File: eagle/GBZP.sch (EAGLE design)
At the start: 30 parts, among them CN1 Battery Connection, J1 AUDIO_JACK_3.5MM_SMD

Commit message: New Silk and New Case files
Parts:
- added C15, C18, C6, C7: 10u, rcl:C-EUC0805
- added C17: 100n, rcl:C-EUC0805
- added C5: 220n, rcl:C-EUC0805
- added C8: 330n, rcl:C-EUC0805
- added C9: 100uF, rcl:CPOL-EU153CLV-0405
- added R7: 27k, GBA:VOLUME
- added R8: 270R, rcl:R-EU_R0805
- added R9: 100k, rcl:R-EU_R0805
- added SP2: SPEAKER, GBA:SPEAKER
- added U4: LM4875, texas:LM4875
- added X2: HEADPHONE, GBA:HEADPHONE
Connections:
- removed net PWM_RIGHT: PI1.GPIO18, R3.1
- new net 5V: C15.1, C17.1, C18.1, C7.2, R7.E, R9.2, U4.VDD
- new net N$11: C6.1, U4.BYP
- new net N$13: C9.-, X2.LEFT, X2.RIGHT
- new net N$14: C9.+, SP2.+, U4.VOUT1
- new net N$15: SP2.-, U4.VOUT2
- new net N$16: R9.1, U4.HPHONE, X2.2
- new net N$5: C5.1, C8.1, R8.2
- new net N$8: R7.S, U4.DC_VOL
- new net N$9: C5.2, U4.VIN
- new net PWM: PI1.GPIO18, R3.1, R8.1
- net GND: now also C15.2, C17.2, C18.2, C6.2, C7.1, C8.2, R7.A, U4.GND, X2.1, X2.GND

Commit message: updates
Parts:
- removed C1: 10uF, adafruit:C-USC0805
- removed C15, C18, C6, C7: 10u, rcl:C-EUC0805
- removed C17: 100n, rcl:C-EUC0805
- removed C5: 220n, rcl:C-EUC0805
- removed C8: 330n, rcl:C-EUC0805
- removed C9: 100uF, rcl:CPOL-EU153CLV-0405
- removed R4: 270Ohm, adafruit:R-US_R0805
- removed R6: 150Ohm, adafruit:R-US_R0805
- removed R7: 27k, GBA:VOLUME
- removed R8: 270R, rcl:R-EU_R0805
- removed R9: 100k, rcl:R-EU_R0805
- removed SP2: SPEAKER, GBA:SPEAKER
- removed U4: LM4875, texas:LM4875
- removed X2: HEADPHONE, GBA:HEADPHONE
- added C10, C11: 100nF, adafruit:C-USC0805
- added C12: 10uF, adafruit:C-USC0805
- added R10: 27k, GBA:VOLUME
- added U1: LM4875, texas:LM4875
- C2: value 10uF -> 100uF; device adafruit:C-USC0805 -> SparkFun-Capacitors:100UF-63V-20%(ELECT)
- C3: value 33nF -> 220nF
- C4: value 33nF -> 330nF
- R5: value 150Ohm -> 270Ohm
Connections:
- removed net 5V: C15.1, C17.1, C18.1, C7.2, R7.E, R9.2, U4.VDD
- removed net N$11: C6.1, U4.BYP
- removed net N$13: C9.-, X2.LEFT, X2.RIGHT
- removed net N$14: C9.+, SP2.+, U4.VOUT1
- removed net N$15: SP2.-, U4.VOUT2
- removed net N$16: R9.1, U4.HPHONE, X2.2
- removed net N$3: C2.1, C3.2, R4.2, R5.2
- removed net N$5: C5.1, C8.1, R8.2
- removed net N$8: R7.S, U4.DC_VOL
- removed net N$9: C5.2, U4.VIN
- new net BYP: C10.1, U1.BYP
- new net DC_VOL: R10.S, U1.DC_VOL
- new net HEADPHONES: J1.RING, J1.TIP, R5.1, U1.HPHONE
- new net VIN: C3.1, U1.VIN
- new net VOUT1: C2.+, SP1.+, U1.VOUT1
- new net VOUT2: SP1.-, U1.VOUT2
- net GND: now also C10.2, R10.A, U1.GND; no longer C15.2, C17.2, C18.2, C3.1, C6.2, C7.1, C8.2, R5.1, R6.2, R7.A, U4.GND, X2.1, X2.GND
- net N$1: now also C2.-, J1.RSH, J1.TSH; no longer C1.2, J1.RING
- net N$2: now also C3.2, C4.2, R3.2; no longer C2.2, J1.TIP
- net N$4: now also C11.2, C12.2, U1.VDD; no longer C1.1, C4.2, R3.2, R6.1
- net PWM: no longer R8.1
- net PWM_LEFT: no longer R4.1
- net SWITCH_OUT+: now also C11.1, C12.1, R10.E, R5.2
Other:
- note added: "AUDIO"
- note removed: "HEADPHONES"
- moved on the sheet: C3, C4, J1, R3, R5, SP1

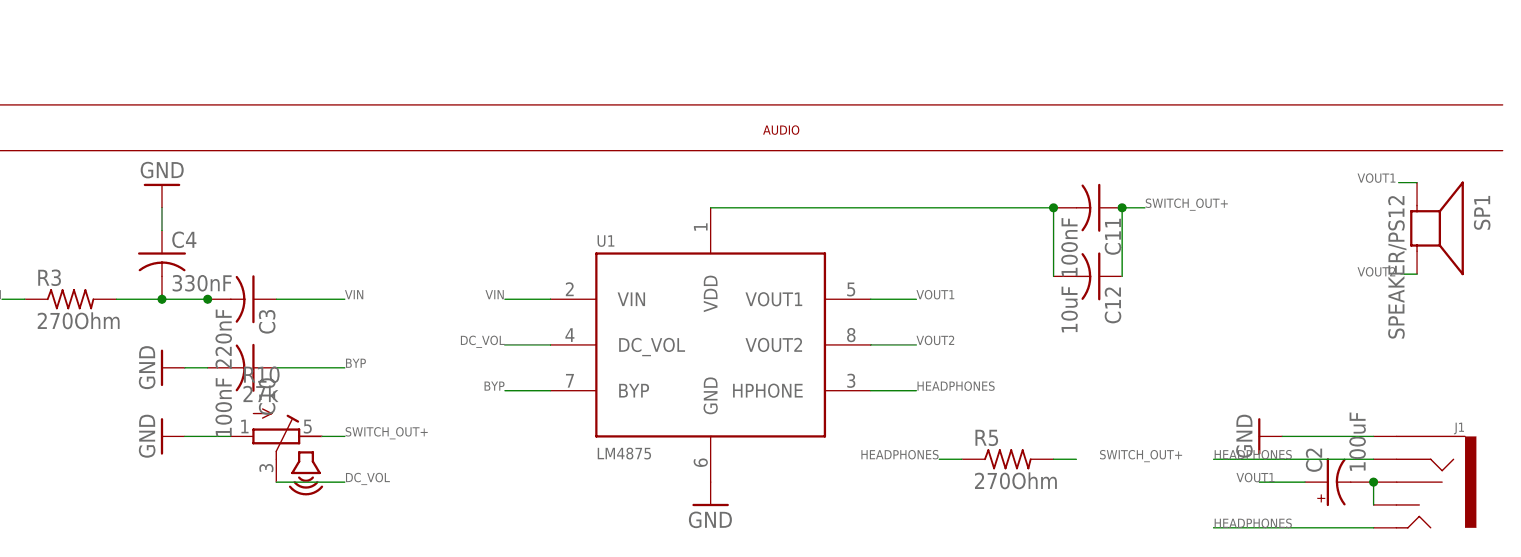
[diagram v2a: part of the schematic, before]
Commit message: added LM4875
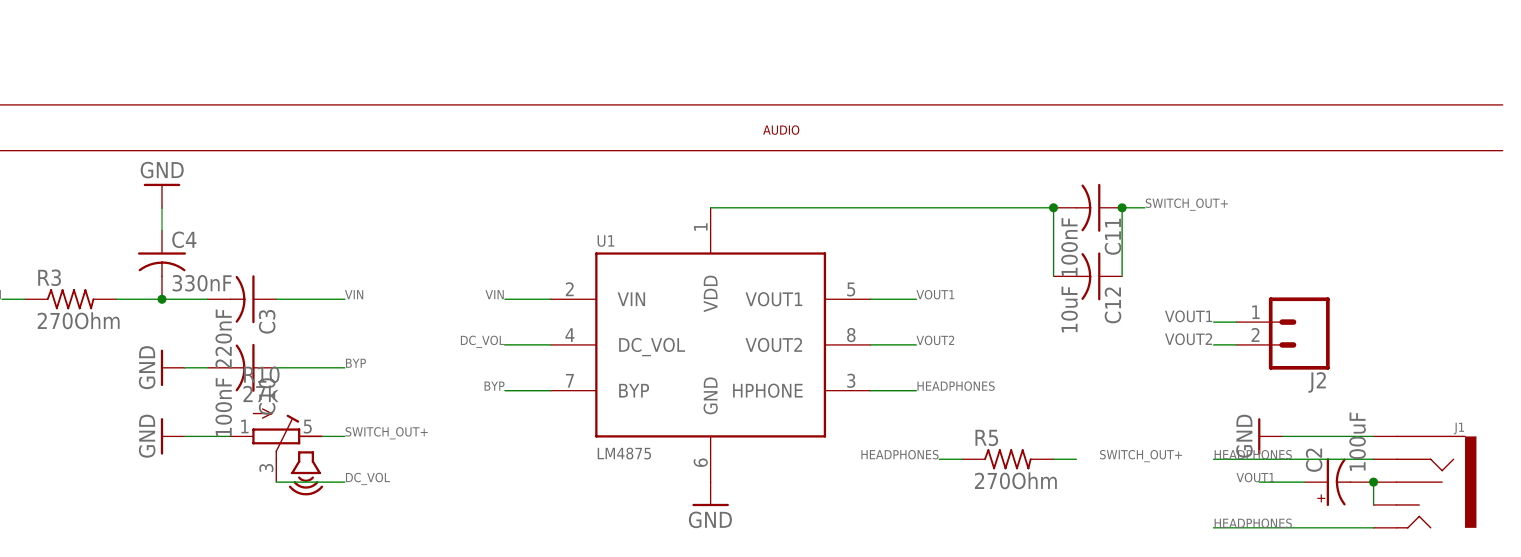
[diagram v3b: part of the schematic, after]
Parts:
- removed SP1: SPEAKER/PS12, adafruit:SPEAKER/PS12
- added J2: (no value), SparkFun-Connectors:CONN_02
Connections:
- net VOUT1: now also J2.1; no longer SP1.+
- net VOUT2: now also J2.2; no longer SP1.-
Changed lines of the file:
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@@
 <part name="GND30" library="supply1" library_urn="urn:adsk.eagle:library:371" deviceset="GND" device=""/>
 <part name="U$1" library="SparkFun-Retired" library_urn="urn:adsk.eagle:library:533" deviceset="SWITCH_SPDT" device=""/>
-<part name="SP1" library="adafruit" library_urn="urn:adsk.eagle:library:420" deviceset="SPEAKER" device="/PS12"/>
 <part name="C2" library="SparkFun-Capacitors" deviceset="100UF-63V-20%(ELECT)" device="" value="100uF"/>
 <part name="U1" library="texas" deviceset="LM4875" device=""/>
@@
 <part name="C11" library="adafruit" library_urn="urn:adsk.eagle:library:420" deviceset="C-US" device="C0805" value="100nF"/>
 <part name="C12" library="adafruit" library_urn="urn:adsk.eagle:library:420" deviceset="C-US" device="C0805" value="10uF"/>
+<part name="J2" library="SparkFun-Connectors" library_urn="urn:adsk.eagle:library:513" deviceset="CONN_02" device="" package3d_urn="urn:adsk.eagle:package:38039/1"/>
 </parts>
 <sheets>
@@
 <instance part="GND30" gate="1" x="175.26" y="43.18" rot="R180"/>
 <instance part="U$1" gate="G$1" x="114.3" y="12.7"/>
-<instance part="SP1" gate="S1" x="314.706" y="38.354" rot="R270"/>
 <instance part="C2" gate="G$1" x="304.8" y="10.16" rot="R90"/>
 <instance part="U1" gate="U$1" x="228.6" y="25.4"/>
@@
 <instance part="C11" gate="G$1" x="279.4" y="40.64" rot="R270"/>
 <instance part="C12" gate="G$1" x="279.4" y="33.02" rot="R270"/>
+<instance part="J2" gate="G$1" x="302.26" y="27.94" rot="R180"/>
 </instances>
 <busses>
@@
 </segment>
 <segment>
-<pinref part="SP1" gate="S1" pin="+"/>
-<wire x1="314.706" y1="43.434" x2="312.674" y2="43.434" width="0.1524" layer="91"/>
-<label x="312.42" y="43.434" size="1.016" layer="95" rot="MR0"/>
+<pinref part="J2" gate="G$1" pin="1"/>
+<wire x1="294.64" y1="27.94" x2="292.1" y2="27.94" width="0.1524" layer="91"/>
+<label x="292.1" y="27.94" size="1.27" layer="95" rot="MR0"/>
 </segment>
 </net>
@@
 <pinref part="R3" gate="G$1" pin="2"/>
 <pinref part="C4" gate="G$1" pin="2"/>
+<wire x1="175.26" y1="30.48" x2="170.18" y2="30.48" width="0.1524" layer="91"/>
 <pinref part="C3" gate="G$1" pin="2"/>
-<junction x="180.34" y="30.48"/>
-<pinref part="C3" gate="G$1" pin="2"/>
-<wire x1="180.34" y1="30.48" x2="175.26" y2="30.48" width="0.1524" layer="91"/>
+<wire x1="175.26" y1="30.48" x2="180.34" y2="30.48" width="0.1524" layer="91"/>
 <junction x="175.26" y="30.48"/>
-<wire x1="175.26" y1="30.48" x2="170.18" y2="30.48" width="0.1524" layer="91"/>
 </segment>
 </net>
@@
 </segment>
 <segment>
-<pinref part="SP1" gate="S1" pin="-"/>
-<wire x1="314.706" y1="33.274" x2="312.928" y2="33.274" width="0.1524" layer="91"/>
-<label x="312.42" y="33.02" size="1.016" layer="95" rot="MR0"/>
-</segment>
-</net>
+<pinref part="J2" gate="G$1" pin="2"/>
+<wire x1="294.64" y1="25.4" x2="292.1" y2="25.4" width="0.1524" layer="91"/>
+<label x="292.1" y="25.4" size="1.27" layer="95" rot="MR0"/>
+</segment>
+</net>

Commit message: headphones
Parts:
- C2: value 100uF -> 10uF; device SparkFun-Capacitors:100UF-63V-20%(ELECT) -> SparkFun-Capacitors:10UF-POLAR-EIA3216-16V-10%(TANT)
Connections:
- net N$1 renamed CAP_LINE_JACK
- net N$4 renamed CAP_LINE
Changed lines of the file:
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@@
 <part name="GND30" library="supply1" library_urn="urn:adsk.eagle:library:371" deviceset="GND" device=""/>
 <part name="U$1" library="SparkFun-Retired" library_urn="urn:adsk.eagle:library:533" deviceset="SWITCH_SPDT" device=""/>
-<part name="C2" library="SparkFun-Capacitors" deviceset="100UF-63V-20%(ELECT)" device="" value="100uF"/>
+<part name="C2" library="SparkFun-Capacitors" library_urn="urn:adsk.eagle:library:510" deviceset="10UF-POLAR" device="-EIA3216-16V-10%(TANT)" package3d_urn="urn:adsk.eagle:package:37418/1" value="10uF"/>
 <part name="U1" library="texas" deviceset="LM4875" device=""/>
 <part name="R5" library="adafruit" library_urn="urn:adsk.eagle:library:420" deviceset="R-US_" device="R0805" value="270Ohm"/>
@@
 </segment>
 </net>
-<net name="N$1" class="0">
+<net name="CAP_LINE_JACK" class="0">
 <segment>
 <pinref part="J1" gate="G$1" pin="RSH"/>
@@
 </segment>
 </net>
-<net name="N$4" class="0">
+<net name="CAP_LINE" class="0">
 <segment>
 <pinref part="C12" gate="G$1" pin="2"/>
